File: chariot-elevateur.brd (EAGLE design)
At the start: 123 x 78 mm, 26 parts, among them CON1 XT-60, Q1 BSS138, U1 WIZ820IO

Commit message: placement connecteurs
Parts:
- VESC: device pinhead:1X03 -> pinhead:1X03/90
- moved CON1 24.8 mm to (37.0, 10.0)
- moved AX12_AR 18.0 mm to (14.0, 14.0), turned to 90 degrees
- moved PHARES_AR 13.0 mm to (24.0, 13.0)
- moved TOF_AR 12.1 mm to (107.0, 17.0), turned to 270 degrees
- moved PHARES_AV 8.60 mm to (24.0, 21.0)
- moved FUMIGENE 8.25 mm to (99.0, 12.0), turned to 180 degrees
- moved JUMPER 7.00 mm to (82.0, 5.00)
- moved VESC 6.71 mm to (90.0, 15.0), turned to 180 degrees
- moved AX12_AV 2.00 mm to (54.0, 10.0)
- moved ENDSTOP 2.00 mm to (51.0, 16.0)
- moved PAS_A_PAS 2.00 mm to (67.0, 10.0)
- moved ENCODEUR_GAUCHE 1.00 mm to (24.0, 5.00)
- moved RASPBERRY 1.00 mm to (42.0, 46.0), turned to 0 degrees

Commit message: end-of-the-day commit
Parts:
- removed RASPBERRY: JST-06, con-jst:GH-06-V
- added C1, C2, C3, C4: 22µF, resistor:C0805
- added C5, C6: 1µF, resistor:C0805
- added D1: DIODE_S15P45, diode_schottky:TO-277A
- added DC1, DC2: TSR 1-2450, dc-dc-converter:SIP3
- added DC3: TSR 2-2450, dc-dc-converter:SIP3
- added DC4: TSR 2-24120, dc-dc-converter:SIP3
- added P1: RG500, polyswitch:5MM
- added R1: 10k, resistor:R0805
- added SJ1: (no value), jumper:SJ_2
- added TOF_AV: JST-08, con-jst:GH-08-V
- moved S1 24.8 mm to (50.0, 41.0), turned to 270 degrees
- moved LED3 24.2 mm to (109.0, 76.0), turned to 180 degrees
- moved R3 21.5 mm to (105.0, 42.0), turned to 0 degrees
- moved R4 18.8 mm to (93.0, 73.0), turned to 0 degrees
- moved ENDSTOP 18.1 mm to (69.0, 18.0)
- moved ENCODEUR_GAUCHE 16.0 mm to (40.0, 5.00)
- moved PHARES_AR 16.0 mm to (40.0, 13.0)
- moved Q1 15.0 mm to (109.0, 42.0)
- moved AX12_AV 15.0 mm to (69.0, 10.0)
- moved R5 14.4 mm to (109.0, 73.0), turned to 0 degrees
- moved R2 14.3 mm to (112.0, 42.0)
- moved CON1 14.0 mm to (23.0, 10.0)
- moved LED2 12.0 mm to (93.0, 76.0), turned to 0 degrees
- moved PAS_A_PAS 11.0 mm to (56.0, 10.0)
- moved PHARES_AV 10.3 mm to (14.5, 25.0), turned to 90 degrees
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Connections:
- removed net +5V: R3.1
- removed net 3.3V: U$1.3.3V, U$1.3.3V3
- removed net AGND: U$1.AGND
- removed net DYN_VCC: AX12_AR.DYN_VCC, AX12_AV.DYN_VCC, FUMIGENE.VCC
- removed net VIN: U$1.VIN
- removed net VIN3V3: U1.VIN1, U1.VIN2
- new net +12V: AX12_AR.DYN_VCC, AX12_AV.DYN_VCC, C5.2, C6.2, SJ1.2
- new net +24V: C1.1, C2.1, C3.1, C4.1, D1.-, DC1.1, DC2.1, DC3.1, DC4.1, S1.VMOT, SJ1.1
- new net +5V/1: DC1.3, ENCODEUR_DROIT.1, ENCODEUR_GAUCHE.1, R3.1, U$1.VIN
- new net +5V/2: DC2.3, PHARES_AR.3, PHARES_AR.4, PHARES_AV.3, PHARES_AV.4
- new net +5V/3: DC3.3
- new net DEL_AR: PHARES_AR.5
- new net DEL_AV: PHARES_AV.5
- new net DIR: S1.DIR, U$1.3
- new net ENC_D_A: ENCODEUR_DROIT.3
- new net ENC_D_B: ENCODEUR_DROIT.4
- new net ENC_G_A: ENCODEUR_GAUCHE.3
- new net ENC_G_B: ENCODEUR_GAUCHE.4
- new net ENDSTOP: ENDSTOP.3
- new net ETH_MISO: U$1.12, U1.MISO
- new net ETH_MOSI: U$1.11, U1.MOSI
- new net ETH_RST: R1.1, U$1.15/A1, U1.RESET
- new net ETH_SCLK: U$1.13, U1.SCLK
- new net ETH_SS: U$1.10, U1.SS
- new net FUM_POMPE: FUMIGENE.VCC
- new net FUM_RES: FUMIGENE.DATA
- new net JUMPER: JUMPER.3
- new net N$1: CON1.(+), P1.P$2
- new net N$10: U$1.25
- new net N$11: U$1.26
- new net N$12: U$1.27
- new net N$13: U$1.28
- new net N$14: U$1.29
- new net N$15: U$1.30
- new net N$16: U$1.31/A12
- new net N$17: U$1.32/A13
- new net N$18: U$1.33/A14
- new net N$19: U$1.34/A15
- new net N$2: PAS_A_PAS.2, S1.1B
- new net N$20: U$1.35/A16
- new net N$21: U$1.36/A17
- new net N$22: U$1.5
- new net N$23: U$1.6
- new net N$24: U$1.24
- new net N$25: U$1.37/A18
- new net N$26: U$1.38/A19
- new net N$3: PAS_A_PAS.3, S1.1A
- new net N$4: D1.+1, D1.+2, P1.P$1
- new net N$5: PAS_A_PAS.4, S1.2A
- new net N$6: PAS_A_PAS.5, S1.2B
- new net N$9: DC4.3, SJ1.3
- new net SCL: LED1.SCL, TOF_AR.4, TOF_AV.4, U$1.19/A5
- new net SDA: LED1.SDA, TOF_AR.3, TOF_AV.3, U$1.18/A4
- new net STEP: S1.STEP, U$1.4
- new net TOF_AR_D: TOF_AR.7
- new net TOF_AR_FD: TOF_AR.8
- new net TOF_AR_FG: TOF_AR.5
- new net TOF_AR_G: TOF_AR.6
- new net TOF_AV_D: TOF_AV.8
- new net TOF_AV_G: TOF_AV.5
- new net TOF_AV_SD: TOF_AV.7
- new net TOF_AV_SG: TOF_AV.6
- new net VESC_CMD: U$1.2, VESC.1
- net +3V3: now also ENDSTOP.2, JUMPER.2, LED1.VCC, S1.VDD, TOF_AR.2, TOF_AV.2, U$1.3.3V, U$1.3.3V3, U1.VIN1, U1.VIN2
- net CHOOSE_COLOR: now also U$1.39/A20
- net GND: now also C1.2, C2.2, C3.2, C4.2, C5.1, C6.1, CON1.(-), DC1.2, DC2.2, DC3.2, DC4.2, ENCODEUR_DROIT.2, ENCODEUR_GAUCHE.2, ENDSTOP.1, JUMPER.1, LED1.GND, PHARES_AR.1, PHARES_AR.2, PHARES_AV.1, PHARES_AV.2, R1.2, S1.GND1, S1.GND2, TOF_AR.1, TOF_AV.1, U$1.AGND, U1.PWDN, VESC.3
- net SERIAL_AX12: now also U$1.0, U$1.1
- net SERIAL_AX12_5V: now also AX12_AR.DATA, AX12_AV.DATA

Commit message: end-of-day commit
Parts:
- renumbered U$1 to TEENSY
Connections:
- removed net N$10: TEENSY.25
- removed net N$13: TEENSY.28
- removed net N$14: TEENSY.29
- removed net N$15: TEENSY.30
- removed net N$16: TEENSY.31/A12
- removed net N$18: TEENSY.33/A14
- removed net N$19: TEENSY.34/A15
- removed net N$20: TEENSY.35/A16
- removed net N$21: TEENSY.36/A17
- removed net N$23: TEENSY.6
- removed net N$24: TEENSY.24
- removed net N$25: TEENSY.37/A18
- removed net N$26: TEENSY.38/A19
- new net FUM_POMPE_CMD: TEENSY.20/A6
- new net FUM_RES_CMD: TEENSY.14/A0
- new net S_MS1: S1.MS1, TEENSY.28
- new net S_MS2: S1.MS2, TEENSY.27
- new net S_MS3: S1.MS3, TEENSY.26
- new net S_N_RST: S1.N_RST, TEENSY.32/A13
- new net S_N_SLEEP: S1.N_SLEEP, TEENSY.31/A12
- net CHOOSE_COLOR: now also TEENSY.8; no longer TEENSY.39/A20
- net DEL_AR: now also TEENSY.6
- net DEL_AV: now also TEENSY.7
- net DIR: now also TEENSY.29; no longer TEENSY.3
- net ENC_D_A: now also TEENSY.39/A20
- net ENC_D_B: now also TEENSY.38/A19
- net ENC_G_A: now also TEENSY.34/A15
- net ENC_G_B: now also TEENSY.33/A14
- net ENDSTOP: now also TEENSY.9
- net JUMPER: now also TEENSY.37/A18
- net N$11: now also TEENSY.4; no longer TEENSY.26
- net N$12: now also TEENSY.3; no longer TEENSY.27
- net N$17: now also TEENSY.2; no longer TEENSY.32/A13
- net STEP: now also TEENSY.30; no longer TEENSY.4
- net TOF_AR_D: now also TEENSY.23/A9
- net TOF_AR_FD: now also TEENSY.16/A2
- net TOF_AR_FG: now also TEENSY.21/A7
- net TOF_AR_G: now also TEENSY.22/A8
- net TOF_AV_D: now also TEENSY.35/A16
- net TOF_AV_G: now also TEENSY.24
- net TOF_AV_SD: now also TEENSY.36/A17
- net TOF_AV_SG: now also TEENSY.25
- net VESC_CMD: now also TEENSY.17/A3; no longer TEENSY.2

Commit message: v1
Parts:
- removed C5, C6: 1µF, resistor:C0805
- added C10, C11, C12, C13: 10µF/50V, resistor:C1210
- added C14, C15: 1µF, resistor:C0805
- added C7, C9: 220µF/25V, resistor:E3,5-8
- added C8: 100µF/50V, resistor:E3,5-8
- added LEVEL_SHIFTER1:Q1, LEVEL_SHIFTER2:Q1, LEVEL_SHIFTER3:Q1, LEVEL_SHIFTER4:Q1, LEVEL_SHIFTER5:Q1: BSS138, transistor-small-signal:SOT23
- added LEVEL_SHIFTER1:R1, LEVEL_SHIFTER1:R2, LEVEL_SHIFTER2:R1, LEVEL_SHIFTER2:R2, LEVEL_SHIFTER3:R1, LEVEL_SHIFTER3:R2, LEVEL_SHIFTER4:R1, LEVEL_SHIFTER4:R2, LEVEL_SHIFTER5:R1, LEVEL_SHIFTER5:R2, R6: 10k, resistor:R0805
- added Q2: DMN2056U, transistor-small-signal:SOT23
- added R7: 100, resistor:R0805
- added USB: (no value), pinhead:1X03
- C1, C2, C3, C4: value 22µF -> 10µF/50V; device resistor:C0805 -> resistor:C1210
- Q1: value BSS138 -> DMN2056U
- R3: value 10k -> 100
- moved C4 92.6 mm to (17.0, 38.0), flipped to the top, turned to 180 degrees
- moved SJ1 85.5 mm to (31.0, 30.0), turned to 180 degrees
- moved DC4 73.9 mm to (31.0, 33.0), turned to 0 degrees
- moved DC2 68.3 mm to (16.0, 41.0), turned to 0 degrees
- moved DC3 42.4 mm to (70.0, 27.0), turned to 180 degrees
- moved C1 30.1 mm to (69.0, 30.0), flipped to the top, turned to 0 degrees
- moved C2 29.0 mm to (69.0, 39.0), flipped to the top, turned to 0 degrees
- moved Q1 25.3 mm to (101.0, 18.0), turned to 180 degrees
- moved R2 23.7 mm to (101.0, 21.0), turned to 180 degrees
- moved C3 21.2 mm to (69.0, 45.0), flipped to the top, turned to 0 degrees
- moved DC1 20.9 mm to (70.0, 42.0), turned to 180 degrees
- moved R3 19.4 mm to (101.0, 23.0)
- moved PHARES_AR 2.00 mm to (40.0, 15.0)
- moved D1 1.00 mm to (33.0, 22.0), turned to 0 degrees
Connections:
- net N$1 renamed V_LIPO
- removed net DEL_AR: PHARES_AR.5, TEENSY.6
- removed net DEL_AV: PHARES_AV.5, TEENSY.7
- removed net FUM_POMPE_CMD: TEENSY.20/A6
- removed net FUM_RES_CMD: TEENSY.14/A0
- removed net N$11: TEENSY.4
- removed net N$12: TEENSY.3
- removed net N$17: TEENSY.2
- removed net N$22: TEENSY.5
- new net CMD_DEL_AR: LEVEL_SHIFTER3:Q1.2, LEVEL_SHIFTER3:R1.2, TEENSY.6
- new net CMD_DEL_AR_5V: LEVEL_SHIFTER3:Q1.3, LEVEL_SHIFTER3:R2.2, PHARES_AR.5
- new net CMD_DEL_AV: LEVEL_SHIFTER2:Q1.2, LEVEL_SHIFTER2:R1.2, TEENSY.7
- new net CMD_DEL_AV_5V: LEVEL_SHIFTER2:Q1.3, LEVEL_SHIFTER2:R2.2, PHARES_AV.5
- new net CMD_FUM_POMPE: R3.1, TEENSY.20/A6
- new net CMD_FUM_RES: R7.1, TEENSY.14/A0
- new net N$10: Q1.1, R2.1, R3.2
- new net N$13: Q2.1, R6.1, R7.2
- new net SCL_5V: LED1.SCL, LEVEL_SHIFTER5:Q1.3, LEVEL_SHIFTER5:R2.2
- new net SDA_5V: LED1.SDA, LEVEL_SHIFTER4:Q1.3, LEVEL_SHIFTER4:R2.2
- new net USB_D+: TEENSY.USBD+, USB.1
- new net USB_D-: TEENSY.USBD-, USB.2
- net +12V: now also C14.2, C15.2; no longer C5.2, C6.2
- net +24V: now also C10.1, C11.1, C12.1, C13.1, C8.+
- net +3V3: now also LEVEL_SHIFTER1:Q1.1, LEVEL_SHIFTER1:R1.1, LEVEL_SHIFTER2:Q1.1, LEVEL_SHIFTER2:R1.1, LEVEL_SHIFTER3:Q1.1, LEVEL_SHIFTER3:R1.1, LEVEL_SHIFTER4:Q1.1, LEVEL_SHIFTER4:R1.1, LEVEL_SHIFTER5:Q1.1, LEVEL_SHIFTER5:R1.1; no longer LED1.VCC, Q1.1, R2.1
- net +5V/1: now also LED1.VCC, LEVEL_SHIFTER1:R2.1, LEVEL_SHIFTER4:R2.1, LEVEL_SHIFTER5:R2.1; no longer R3.1
- net +5V/2: now also C7.+, LEVEL_SHIFTER2:R2.1, LEVEL_SHIFTER3:R2.1
- net +5V/3: now also C9.+, FUMIGENE.VCC
- net FUM_POMPE: now also FUMIGENE.GND, Q1.3; no longer FUMIGENE.VCC
- net FUM_RES: now also Q2.3
- net GND: now also C10.2, C11.2, C12.2, C13.2, C14.1, C15.1, C7.-, C8.-, C9.-, Q1.2, Q2.2, R2.2, R6.2, USB.3; no longer C5.1, C6.1, FUMIGENE.GND
- net SCL: now also LEVEL_SHIFTER5:Q1.2, LEVEL_SHIFTER5:R1.2; no longer LED1.SCL
- net SDA: now also LEVEL_SHIFTER4:Q1.2, LEVEL_SHIFTER4:R1.2; no longer LED1.SDA
- net SERIAL_AX12: now also LEVEL_SHIFTER1:Q1.2, LEVEL_SHIFTER1:R1.2; no longer Q1.2, R2.2
- net SERIAL_AX12_5V: now also LEVEL_SHIFTER1:Q1.3, LEVEL_SHIFTER1:R2.2; no longer Q1.3, R3.2
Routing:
- net +3V3: track 0.00 -> 334.3 mm, vias 0 -> 5
- net +5V/1: track 0.00 -> 245.3 mm, vias 0 -> 3
- net SERIAL_AX12_5V: track 0.00 -> 142.8 mm, vias 0 -> 1
- net CMD_DEL_AV: track 0.00 -> 122.9 mm, vias 0 -> 1
- net SDA: track 0.00 -> 109.2 mm, vias 0 -> 2
- net SCL: track 0.00 -> 109.1 mm, vias 0 -> 3
- net +24V: track 0.00 -> 107.0 mm
- net ETH_RST: track 0.00 -> 104.3 mm, vias 0 -> 1
- net CMD_DEL_AR: track 0.00 -> 100.1 mm, vias 0 -> 1
- net ETH_MISO: track 0.00 -> 86.5 mm
- net +12V: track 0.00 -> 86.4 mm, vias 0 -> 1
- net ETH_SCLK: track 0.00 -> 78.1 mm, vias 0 -> 1
- net +5V/2: track 0.00 -> 69.6 mm
- net ETH_SS: track 0.00 -> 69.4 mm
- net ETH_MOSI: track 0.00 -> 65.5 mm
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- added copper zone on layer 1, net GND
- added copper zone on layer 16, net GND

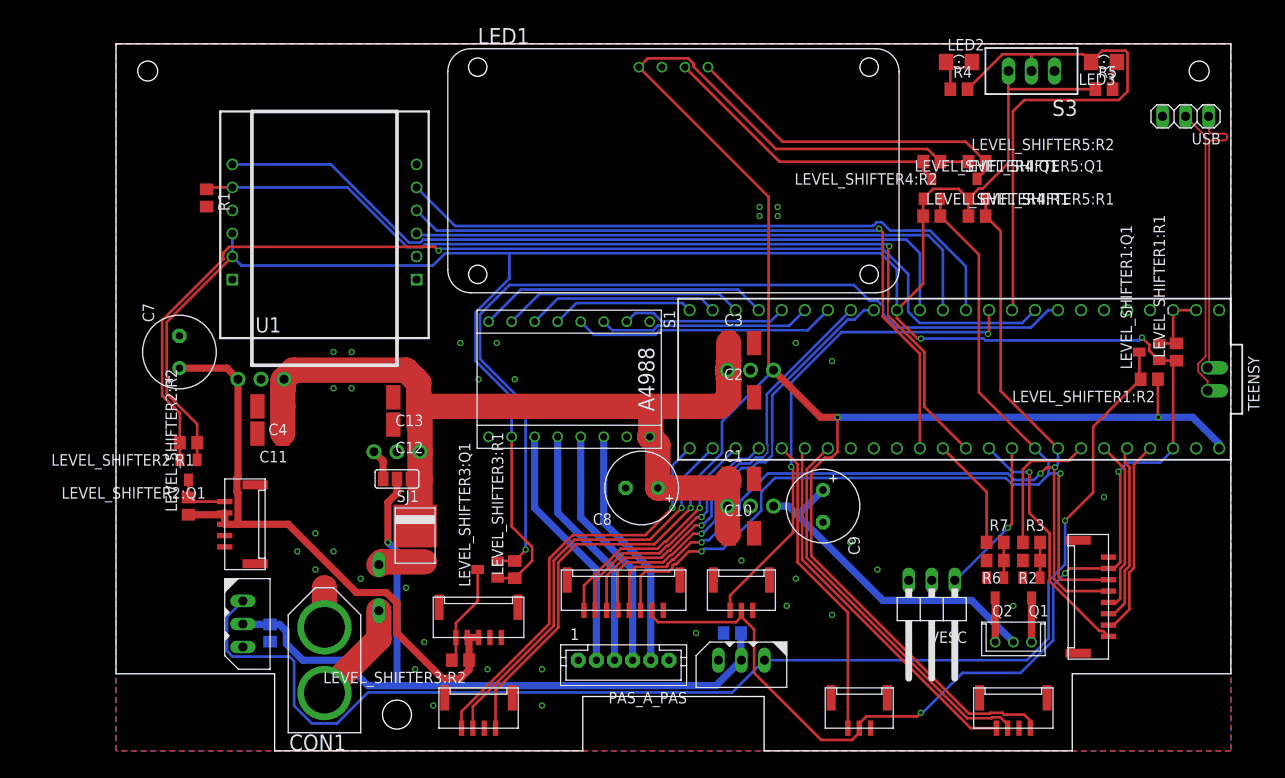
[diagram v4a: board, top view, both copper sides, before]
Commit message: Update components ref + add debug LEDs + map unused pins for debug
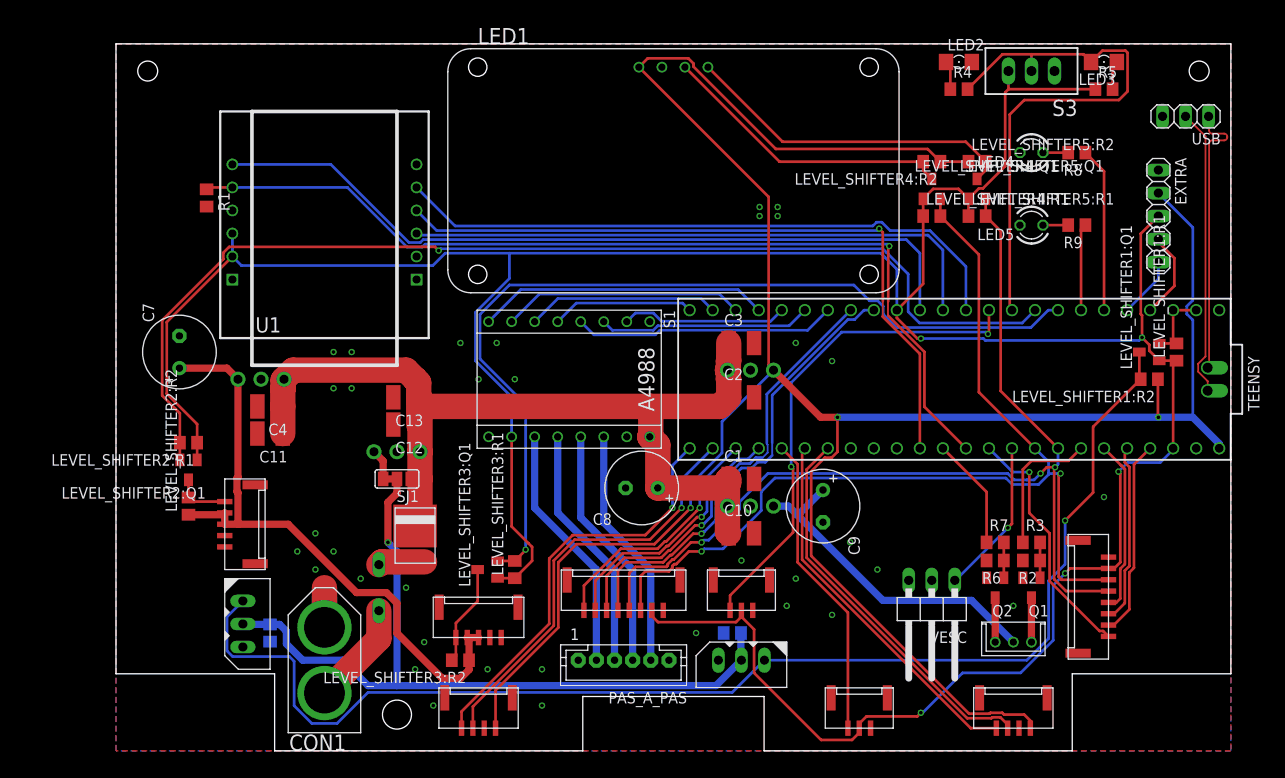
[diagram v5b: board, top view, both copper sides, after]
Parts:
- added EXTRA: (no value), pinhead:1X05
- added LED4: red, led:LED3MM
- added LED5: orange, led:LED3MM
- added R8, R9: 330, resistor:R0805
- LED2: value green -> blue
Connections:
- new net DEL_ERROR: R8.1, TEENSY.4
- new net DEL_WARNING: R9.1, TEENSY.5
- new net EXTRA_GPIO_1: EXTRA.4, TEENSY.2
- new net EXTRA_GPIO_2: EXTRA.5, TEENSY.3
- new net N$1: LED4.A, R8.2
- new net N$11: LED5.A, R9.2
- net +3V3: now also EXTRA.3
- net +5V/1: now also EXTRA.2
- net GND: now also EXTRA.1, LED4.K, LED5.K
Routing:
- net +5V/1: track 245.3 -> 272.2 mm
- net DEL_ERROR: track 0.00 -> 18.2 mm
- net +3V3: track 334.3 -> 348.6 mm
- net EXTRA_GPIO_1: track 0.00 -> 9.68 mm
- net DEL_WARNING: track 0.00 -> 9.58 mm
- net EXTRA_GPIO_2: track 0.00 -> 6.73 mm
- net N$11: track 0.00 -> 2.78 mm
- net N$1: track 0.00 -> 2.78 mm
- net N$9: track 3.42 -> 4.94 mm
